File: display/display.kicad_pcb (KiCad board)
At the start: 2 copper layers, 19 parts, among them J1 DIN41612_03x32_ABC

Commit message: Layout is ongoing
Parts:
- N1, N2, N3, N4, N5, N6: moved to B.Cu
- moved R7 52.3 mm to (212.6, 105.8)
- moved R2 44.2 mm to (98.4, 29.7), turned to 180 degrees
- moved R5 43.6 mm to (195.3, 29.5), turned to 180 degrees
- moved R1 43.5 mm to (75.3, 29.6), turned to 180 degrees
- moved R4 43.1 mm to (157.2, 29.6), turned to 180 degrees
- moved R6 42.2 mm to (218.5, 29.5), turned to 180 degrees
- moved R3 41.9 mm to (133.9, 29.6), turned to 180 degrees
- moved R8 34.1 mm to (212.0, 94.9)
- moved J1 19.7 mm to (180.4, 122.0)
- moved N5 18.8 mm to (188.2, 56.0)
- moved D3 17.7 mm to (110.0, 53.4)
- moved D4 17.7 mm to (110.0, 60.8)
- moved N3 17.3 mm to (129.5, 55.4)
- moved N4 17.3 mm to (152.7, 55.4)
- moved N6 17.3 mm to (214.1, 54.9)
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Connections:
- J1 pad c1: /T4-0 -> /T6-6
- J1 pad c10: /T4-9 -> /T6-5
- J1 pad c11: /T5-0 -> /T5-9
- J1 pad c12: /T5-1 -> /T5-8
- J1 pad c13: /T5-2 -> /T5-7
- J1 pad c14: /T5-3 -> /T5-6
- J1 pad c15: /T5-4 -> /T5-5
- J1 pad c16: /T5-5 -> /T5-4
- J1 pad c17: /T5-6 -> /T5-3
- J1 pad c18: /T5-7 -> /T5-2
- J1 pad c19: /T5-8 -> /T5-1
- J1 pad c2: /T4-1 -> /T6-7
- J1 pad c20: /T5-9 -> /T5-0
- J1 pad c21: /T6-0 -> /T4-9
- J1 pad c22: /T6-1 -> /T4-8
- J1 pad c23: /T6-2 -> /T4-7
- J1 pad c24: /T6-3 -> /T4-6
- J1 pad c25: /T6-4 -> /T4-5
- J1 pad c26: /T6-5 -> /T4-4
- J1 pad c27: /T6-6 -> /T4-3
- J1 pad c28: /T6-7 -> /T4-2
- J1 pad c29: /T6-8 -> /T4-1
- J1 pad c3: /T4-2 -> /T6-8
- J1 pad c30: /T6-9 -> /T4-0
- J1 pad c4: /T4-3 -> /T6-9
- J1 pad c5: /T4-4 -> /T6-0
- J1 pad c6: /T4-5 -> /T6-1
- J1 pad c7: /T4-6 -> /T6-2
- J1 pad c8: /T4-7 -> /T6-3
- J1 pad c9: /T4-8 -> /T6-4
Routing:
- net /T6-6: track 0.00 -> 48.5 mm
- net Net-(N6-A): track 0.00 -> 42.9 mm
- net /T6-7: track 0.00 -> 42.9 mm
- net /T6-8: track 0.00 -> 33.0 mm
- net /T6-5: track 0.00 -> 29.0 mm
- net /T6-9: track 0.00 -> 26.1 mm
- net /T6-4: track 0.00 -> 23.4 mm
- net /T6-0: track 0.00 -> 19.7 mm
- net /T6-3: track 0.00 -> 18.4 mm
- net /T6-2: track 0.00 -> 13.4 mm
- net /T6-1: track 0.00 -> 10.8 mm
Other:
- board outline added: 177 x 107.2 mm

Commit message: Additional minor tweaking
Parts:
- moved N5 3.76 mm to (191.8, 54.9)
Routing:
- net Net-(N6-A): track 42.9 -> 42.2 mm
- net /T6-7: track 42.9 -> 42.3 mm
- net /T6-6: track 48.5 -> 48.0 mm
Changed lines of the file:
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@@
 	(footprint "hatsunearu:IN_12B_Socket"
 		(layer "B.Cu")
-		(at 188.181835 56.0474)
+		(at 191.7604 54.8894)
 		(property "Reference" "N5"
 			(at 0 -11.75 0)
@@
 	)
 	(segment
-		(start 224.554635 49.4858)
-		(end 224.554635 65.5386)
+		(start 223.901 48.832165)
+		(end 223.901 66.192235)
+		(width 0.2)
+		(layer "F.Cu")
+		(net 21)
+	)
+	(segment
+		(start 214.050461 45.9468)
+		(end 215.440858 44.556403)
+		(width 0.2)
+		(layer "F.Cu")
+		(net 21)
+	)
+	(segment
+		(start 223.901 66.192235)
+		(end 210.889435 79.2038)
+		(width 0.2)
+		(layer "F.Cu")
+		(net 21)
+	)
+	(segment
+		(start 219.625238 44.556403)
+		(end 223.901 48.832165)
 		(width 0.2)
 		(layer "F.Cu")
@@
 	)
 	(segment
-		(start 214.050461 45.9468)
-		(end 215.440858 44.556403)
-		(width 0.2)
-		(layer "F.Cu")
-		(net 21)
-	)
-	(segment
-		(start 224.554635 65.5386)
-		(end 210.889435 79.2038)
-		(width 0.2)
-		(layer "F.Cu")
-		(net 21)
-	)
-	(segment
-		(start 219.625238 44.556403)
-		(end 224.554635 49.4858)
-		(width 0.2)
-		(layer "F.Cu")
-		(net 21)
-	)
-	(segment
-		(start 222.929035 53.575374)
-		(end 222.929035 64.548)
+		(start 219.800461 50.4468)
+		(end 222.5548 53.201139)
 		(width 0.2)
 		(layer "F.Cu")
@@
 	)
 	(segment
-		(start 219.800461 50.4468)
-		(end 222.929035 53.575374)
+		(start 222.5548 53.201139)
+		(end 222.5548 64.922235)
 		(width 0.2)
 		(layer "F.Cu")
@@
 	)
 	(segment
-		(start 222.929035 64.548)
+		(start 222.5548 64.922235)
 		(end 210.508435 76.9686)
 		(width 0.2)
@@
 	)
 	(segment
-		(start 223.868835 64.8274)
-		(end 210.610035 78.0862)
-		(width 0.2)
-		(layer "F.Cu")
-		(net 31)
-	)
-	(segment
-		(start 223.868835 50.841294)
-		(end 223.868835 64.8274)
-		(width 0.2)
-		(layer "F.Cu")
-		(net 31)
-	)
-	(segment
-		(start 219.974341 46.9468)
-		(end 223.868835 50.841294)
-		(width 0.2)
-		(layer "F.Cu")
-		(net 31)
-	)
-	(segment
 		(start 218.050461 46.9468)
 		(end 219.974341 46.9468)
@@
 	)
 	(segment
+		(start 219.974341 46.9468)
+		(end 223.1898 50.162259)
+		(width 0.2)
+		(layer "F.Cu")
+		(net 31)
+	)
+	(segment
+		(start 223.1898 65.506435)
+		(end 210.610035 78.0862)
+		(width 0.2)
+		(layer "F.Cu")
+		(net 31)
+	)
+	(segment
 		(start 218.050461 46.9468)
 		(end 216.833035 48.164226)
@@
 	)
 	(segment
+		(start 223.1898 50.162259)
+		(end 223.1898 65.506435)
+		(width 0.2)
+		(layer "F.Cu")
+		(net 31)
+	)
+	(segment
 		(start 218.050461 46.9468)
 		(end 217.341035 47.656226)
@@
 	)
 	(segment
-		(start 225.545235 36.5276)
-		(end 225.545235 61.2206)
+		(start 218.513635 29.496)
+		(end 224.6884 35.670765)
 		(width 0.2)
 		(layer "B.Cu")
@@
 	)
 	(segment
-		(start 218.513635 29.496)
-		(end 225.545235 36.5276)
+		(start 224.6884 35.670765)
+		(end 224.6884 62.077435)
 		(width 0.2)
 		(layer "B.Cu")
@@
 	)
 	(segment
-		(start 225.545235 61.2206)
+		(start 224.6884 62.077435)
 		(end 223.819035 62.9468)
 		(width 0.2)

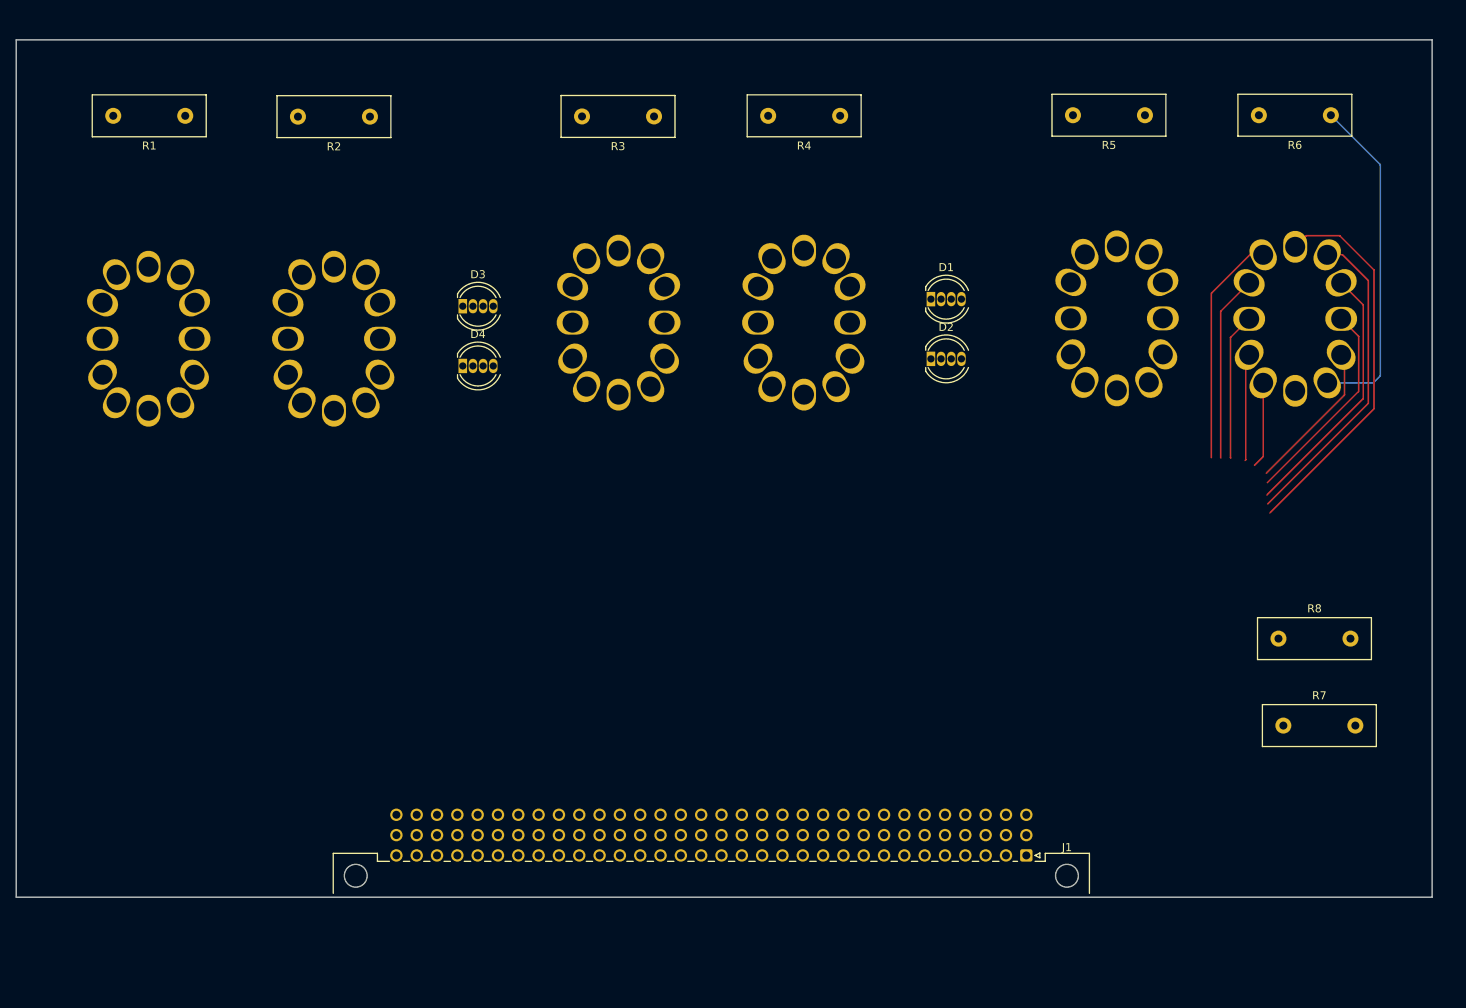
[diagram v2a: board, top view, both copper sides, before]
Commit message: Clean up symbol library references to be local to repo
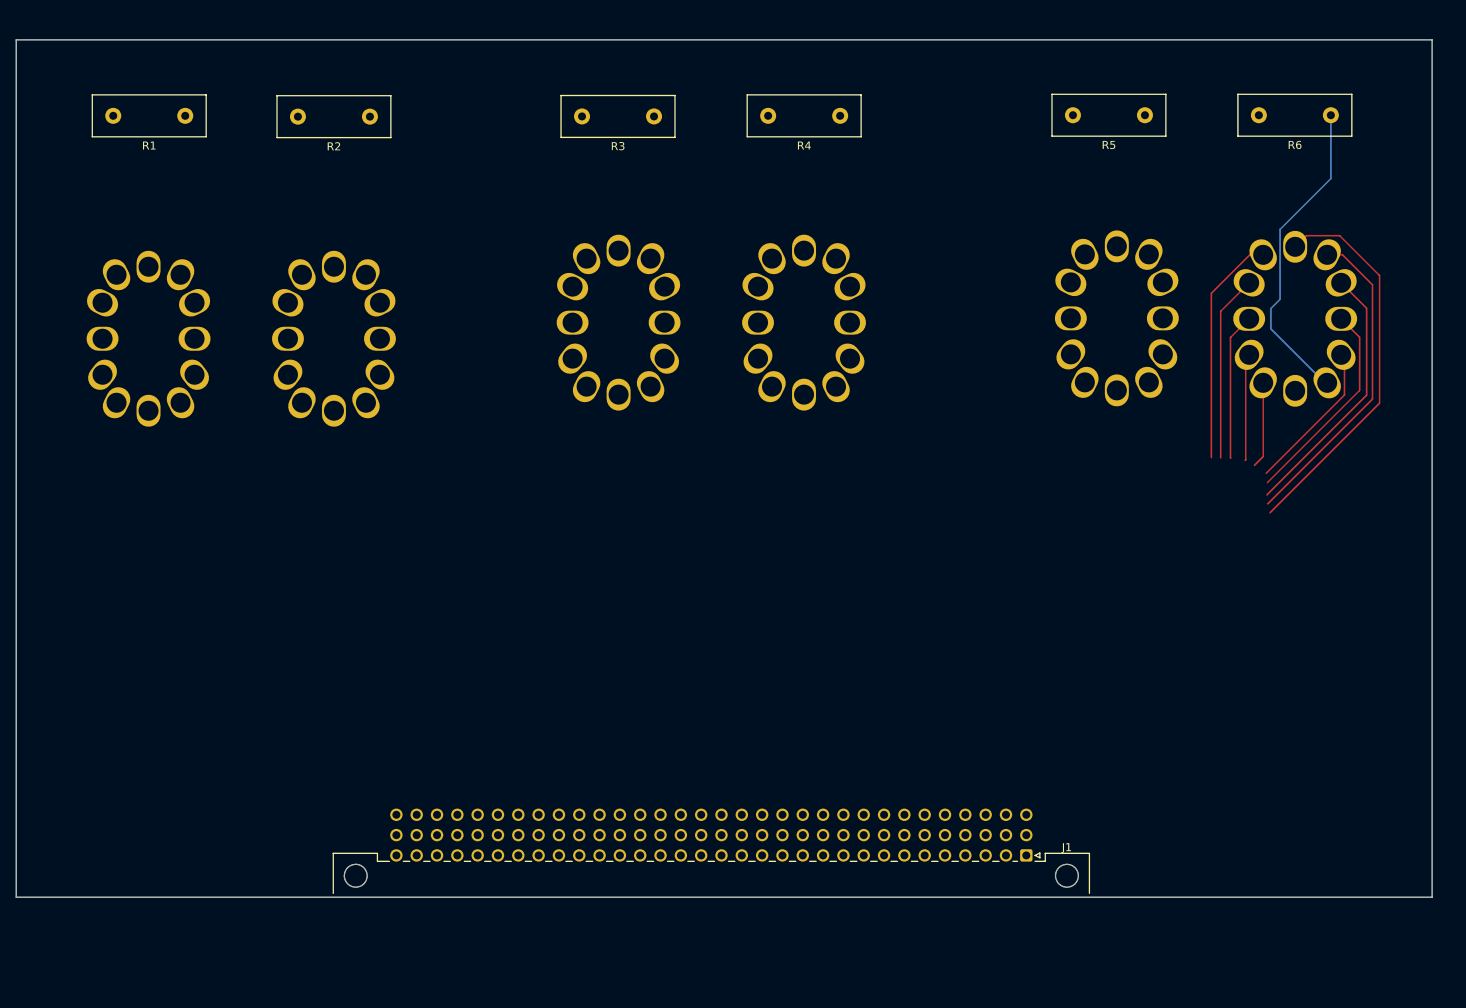
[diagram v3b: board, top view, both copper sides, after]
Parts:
- removed D1, D2, D3, D4: LED_RABG, LED_THT:LED_D5.0mm-4_RGB
- removed R7, R8: 0 ohm, Resistor_THT:R_Box_L14.0mm_W5.0mm_P9.00mm
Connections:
- J1 pad a1: Net-(J1-Pin_a1) -> unconnected-(J1-Pin_a1-Pada1)
- J1 pad a2: Net-(J1-Pin_a1) -> unconnected-(J1-Pin_a2-Pada2)
- J1 pad b10: GND -> Net-(J1-Pin_b1)
- J1 pad b11: GND -> Net-(J1-Pin_b1)
- J1 pad b12: GND -> Net-(J1-Pin_b1)
- J1 pad b13: GND -> Net-(J1-Pin_b1)
- J1 pad b14: GND -> Net-(J1-Pin_b1)
- J1 pad b15: GND -> Net-(J1-Pin_b1)
- J1 pad b16: GND -> Net-(J1-Pin_b1)
- J1 pad b17: GND -> Net-(J1-Pin_b1)
- J1 pad b18: GND -> Net-(J1-Pin_b1)
- J1 pad b19: GND -> Net-(J1-Pin_b1)
- J1 pad b20: GND -> Net-(J1-Pin_b1)
- J1 pad b21: GND -> Net-(J1-Pin_b1)
- J1 pad b22: GND -> Net-(J1-Pin_b1)
- J1 pad b23: GND -> Net-(J1-Pin_b1)
- J1 pad b24: GND -> Net-(J1-Pin_b1)
- J1 pad b25: unconnected-(J1-Pin_b25-Padb25) -> Net-(J1-Pin_b1)
- J1 pad b26: unconnected-(J1-Pin_b26-Padb26) -> Net-(J1-Pin_b1)
- J1 pad b27: Net-(D3-BK) -> Net-(J1-Pin_b1)
- J1 pad b28: Net-(D3-GK) -> Net-(J1-Pin_b1)
- J1 pad b29: Net-(D3-RK) -> Net-(J1-Pin_b1)
- J1 pad b30: Net-(D1-BK) -> Net-(J1-Pin_b1)
- J1 pad b31: Net-(D1-GK) -> Net-(J1-Pin_b1)
- J1 pad b32: Net-(D1-RK) -> Net-(J1-Pin_b1)
- J1 pad b8: GND -> Net-(J1-Pin_b1)
- J1 pad b9: GND -> Net-(J1-Pin_b1)
- J1 pad c31: Net-(D1-A) -> unconnected-(J1-Pin_c31-Padc31)
- J1 pad c32: Net-(D1-A) -> unconnected-(J1-Pin_c32-Padc32)
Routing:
- net Net-(N6-A): track 42.2 -> 39.7 mm
- net /T6-6: track 48.0 -> 48.5 mm

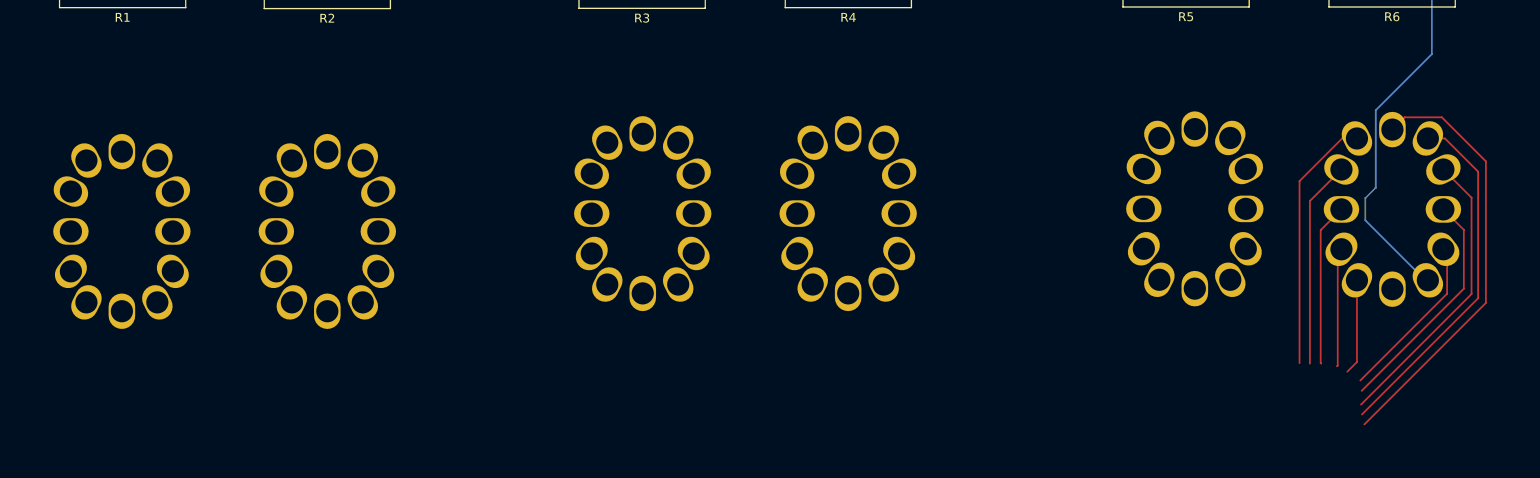
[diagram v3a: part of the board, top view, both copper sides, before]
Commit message: Add Nixie socket to NixComp lib and update PCB
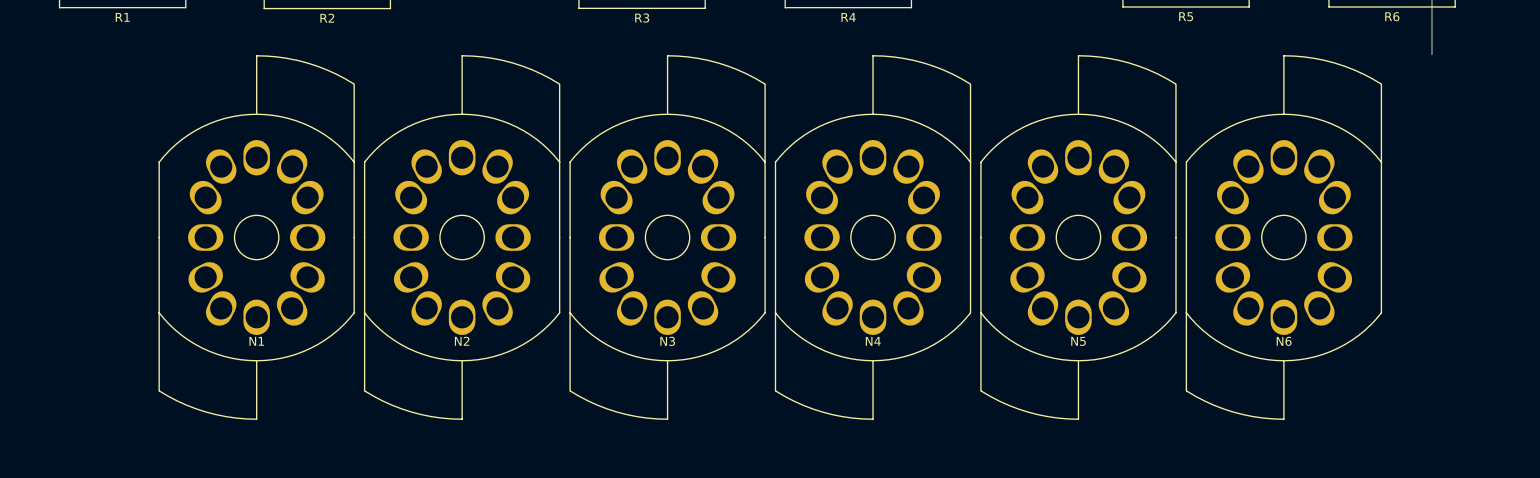
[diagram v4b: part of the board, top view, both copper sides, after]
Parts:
- N1, N2, N3, N4, N5, N6: footprint hatsunearu:IN_12B_Socket -> NixComp:IN_12B_Socket; moved to F.Cu
- moved N1 15.2 mm to (85.9, 58.1)
- moved N2 15.2 mm to (109.1, 58.1)
- moved N5 13.5 mm to (178.6, 58.1)
- moved N6 12.6 mm to (201.8, 58.1)
- moved N4 3.89 mm to (155.5, 58.1)
- moved N3 3.89 mm to (132.3, 58.1)
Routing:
- net /T6-6: track 48.5 -> 0.00 mm
- net /T6-7: track 42.8 -> 0.00 mm
- net /T6-8: track 33.0 -> 0.00 mm
- net Net-(N6-A): track 39.7 -> 7.99 mm
- net /T6-5: track 29.0 -> 0.00 mm
- net /T6-9: track 26.2 -> 0.00 mm
- net /T6-4: track 23.4 -> 0.00 mm
- net /T6-0: track 19.7 -> 0.00 mm
- net /T6-3: track 18.4 -> 0.00 mm
- net /T6-2: track 13.4 -> 0.00 mm
- net /T6-1: track 10.8 -> 0.00 mm

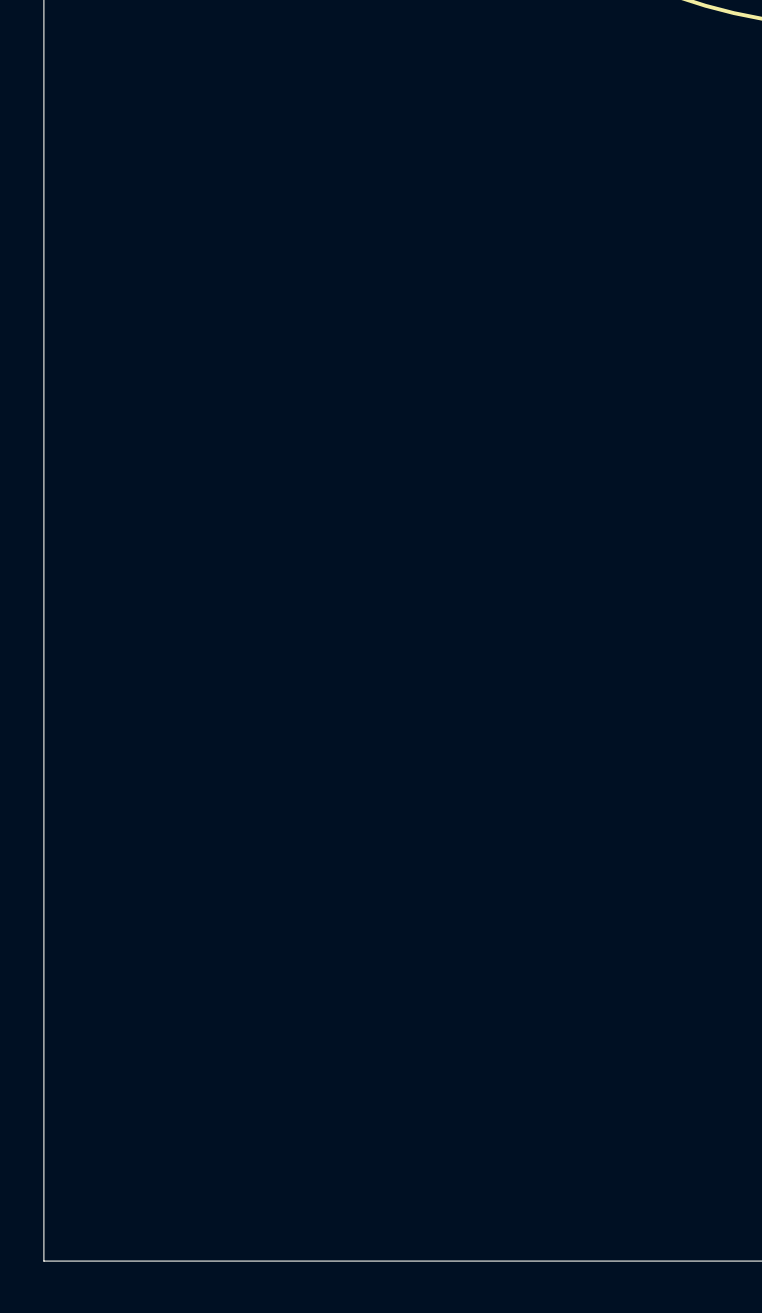
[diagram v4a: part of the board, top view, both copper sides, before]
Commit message: Ongoing development. Add shunt resistors to display board.
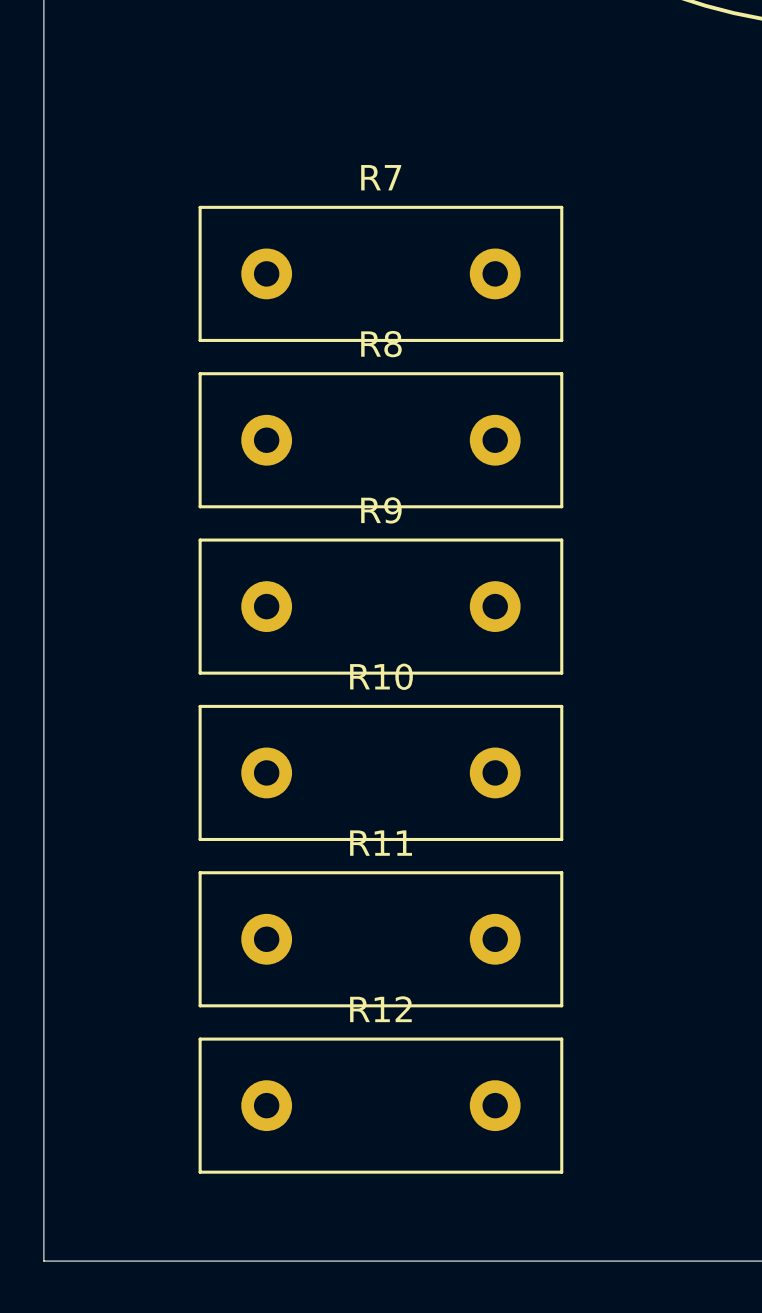
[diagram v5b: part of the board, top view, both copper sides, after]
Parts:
- added R10: 15K, Resistor_THT:R_Box_L14.0mm_W5.0mm_P9.00mm, F.Cu at (63.0, 108.0)
- added R11: 15K, Resistor_THT:R_Box_L14.0mm_W5.0mm_P9.00mm, F.Cu at (63.0, 114.6)
- added R12: 15K, Resistor_THT:R_Box_L14.0mm_W5.0mm_P9.00mm, F.Cu at (63.0, 121.1)
- added R7: 15K, Resistor_THT:R_Box_L14.0mm_W5.0mm_P9.00mm, F.Cu at (63.0, 88.4)
- added R8: 15K, Resistor_THT:R_Box_L14.0mm_W5.0mm_P9.00mm, F.Cu at (63.0, 94.9)
- added R9: 15K, Resistor_THT:R_Box_L14.0mm_W5.0mm_P9.00mm, F.Cu at (63.0, 101.5)
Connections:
- J1 pad a1: unconnected-(J1-Pin_a1-Pada1) -> Net-(J1-Pin_a1)
- J1 pad a2: unconnected-(J1-Pin_a2-Pada2) -> Net-(J1-Pin_a2)
- J1 pad c31: unconnected-(J1-Pin_c31-Padc31) -> Net-(J1-Pin_c31)
- J1 pad c32: unconnected-(J1-Pin_c32-Padc32) -> Net-(J1-Pin_c32)
